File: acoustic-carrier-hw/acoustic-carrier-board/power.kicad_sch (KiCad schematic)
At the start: 88 parts, among them IC1 ECP5-BGA256, J3 Conn_02x08_Odd_Even, U10 TLV62569DBV, U11 TLV62569DBV, U14 TLV62569DBV, U5 OPA376xxDBV, U8 TLV62569DBV

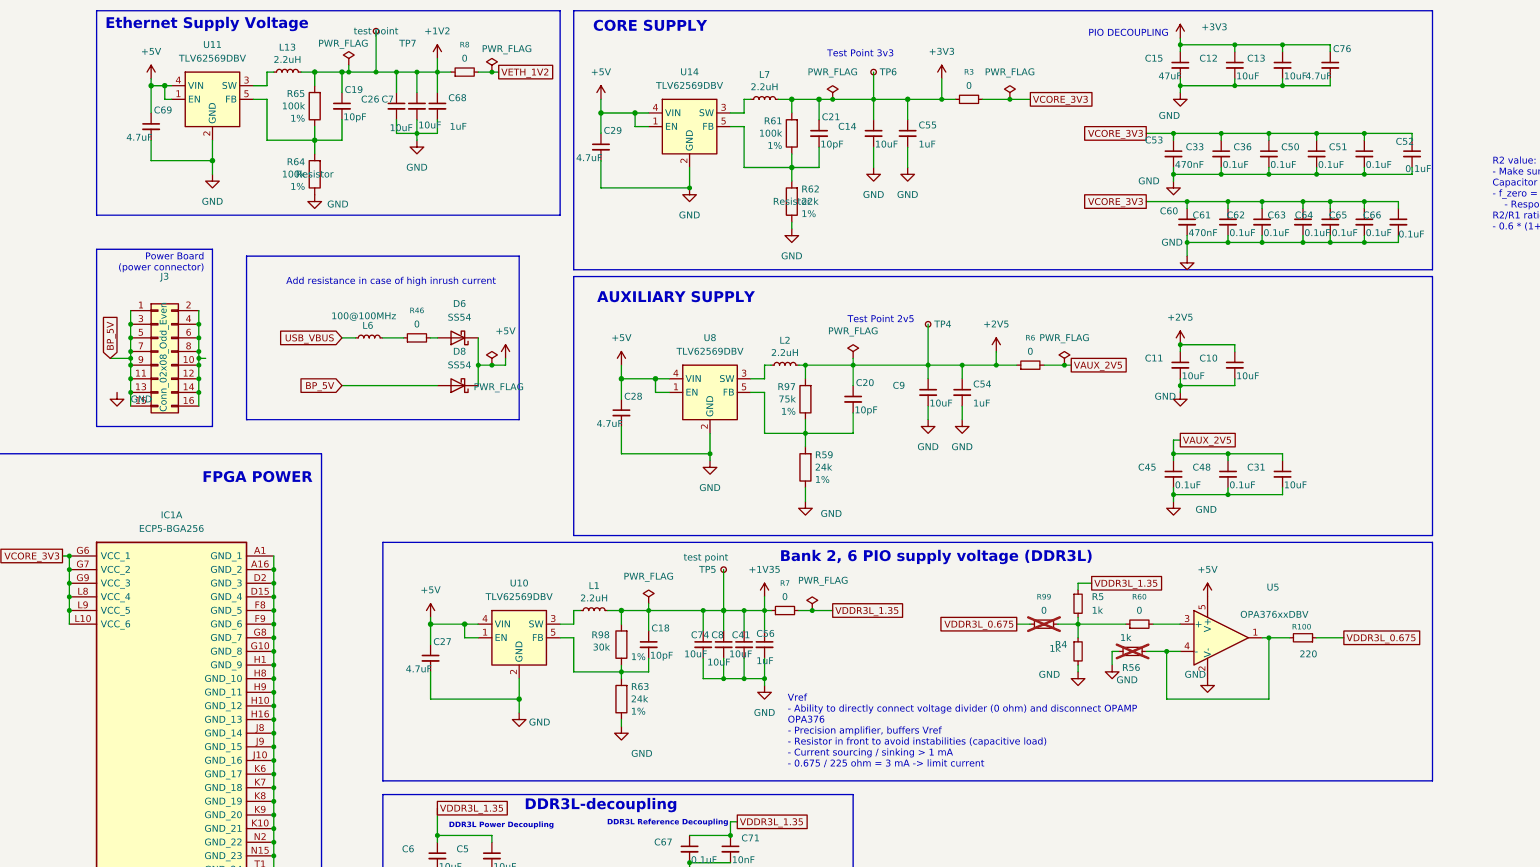
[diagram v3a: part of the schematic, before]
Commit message: [carrier] Checked power-supply part (next) check ethernet-board
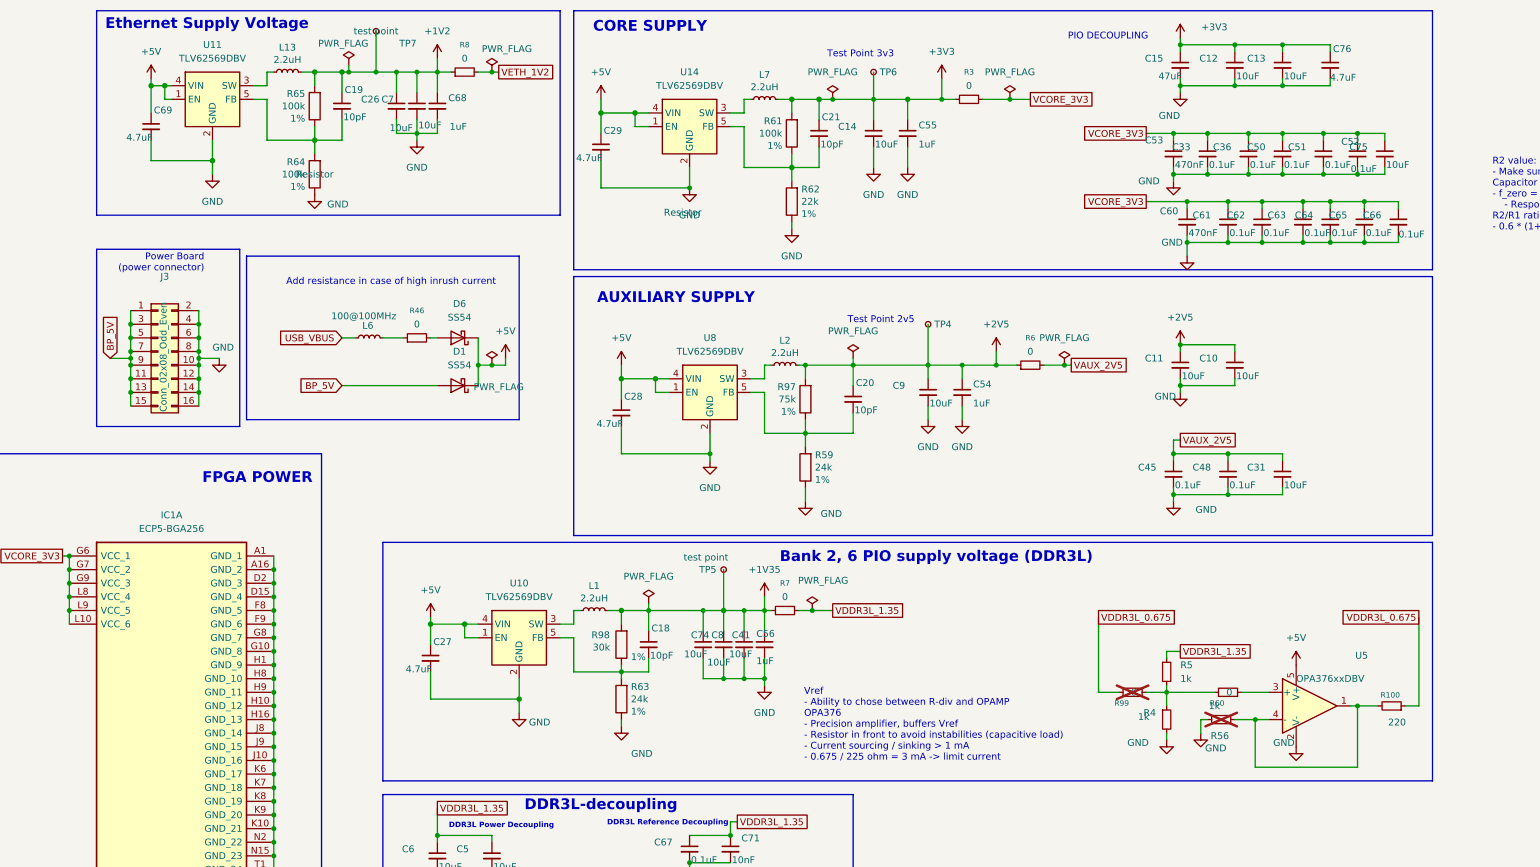
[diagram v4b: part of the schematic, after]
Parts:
- removed D8: SS54, Diode_SMD:D_SMA-SMB_Universal_Handsoldering, symbol Device:D_Schottky
- added C75: 10uF, Capacitor_SMD:C_0603_1608Metric, symbol Device:C_Small
- added D1: SS54, Diode_SMD:D_SMA, symbol Device:D_Schottky
- D6: footprint Diode_SMD:D_SMA-SMB_Universal_Handsoldering -> Diode_SMD:D_SMA
- R60, R99: footprint Resistor_SMD:R_0805_2012Metric_Pad1.20x1.40mm_HandSolder -> Resistor_SMD:R_0603_1608Metric; LPN C17477 -> C21189; MPN 0805W8F0000T5E -> 0603WAF0000T5E
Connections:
- net +5V: now also D1.1 (K)
- net BP_5V: now also D1.2 (A)
- net GND: now also J3.10 (Pin_10), J3.12 (Pin_12), J3.14 (Pin_14), J3.16 (Pin_16), J3.2 (Pin_2), J3.4 (Pin_4), J3.6 (Pin_6), J3.8 (Pin_8), C75.2
- net VCORE_3V3: now also C75.1
- net VDDR3L_0.675: now also R99.2; no longer R99.1
- net at R4.1, R5.2: now also R60.2, R99.1; no longer R60.1, R99.2
- net at U5.3 (+): now also R60.1; no longer R60.2
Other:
- note added: "Vref - Ability to chose between R-div and OPAMP OPA376 - Precision amplifier, buffers Vref - Resistor in front to avoid instabilities (capacitive load) - Current sourcing / sinking > 1 mA - 0.675 / 225 ohm = 3 mA -> limit current"
- note removed: "Vref - Ability to directly connect voltage divider (0 ohm) and disconnect OPAMP OPA376 - Precision amplifier, buffers Vref - Resistor in front to avoid instabilities (capacitive load) - Current sourcing / sinking > 1 mA - 0.675 / 225 ohm = 3 mA -> limit current"
- moved on the sheet: C33, C36, C50, C51, C52, R100, R4, R5, R56, U5

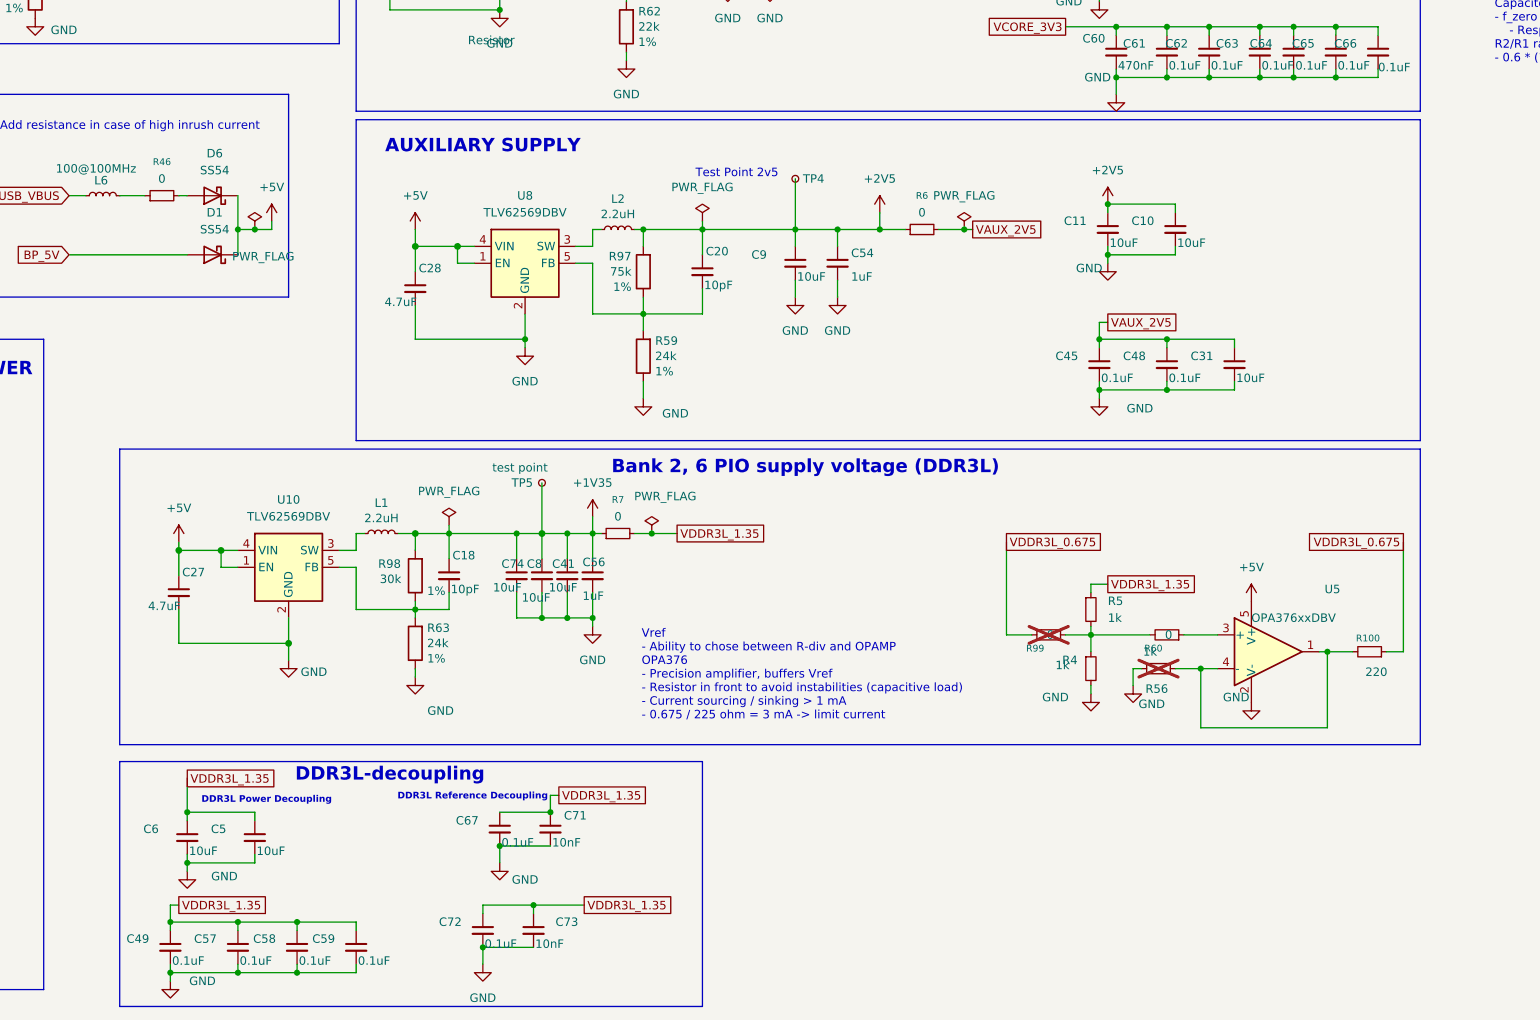
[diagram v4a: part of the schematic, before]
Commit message: [carrier] Added separate buses for ddr3 ctrl-cmd and dq-groups
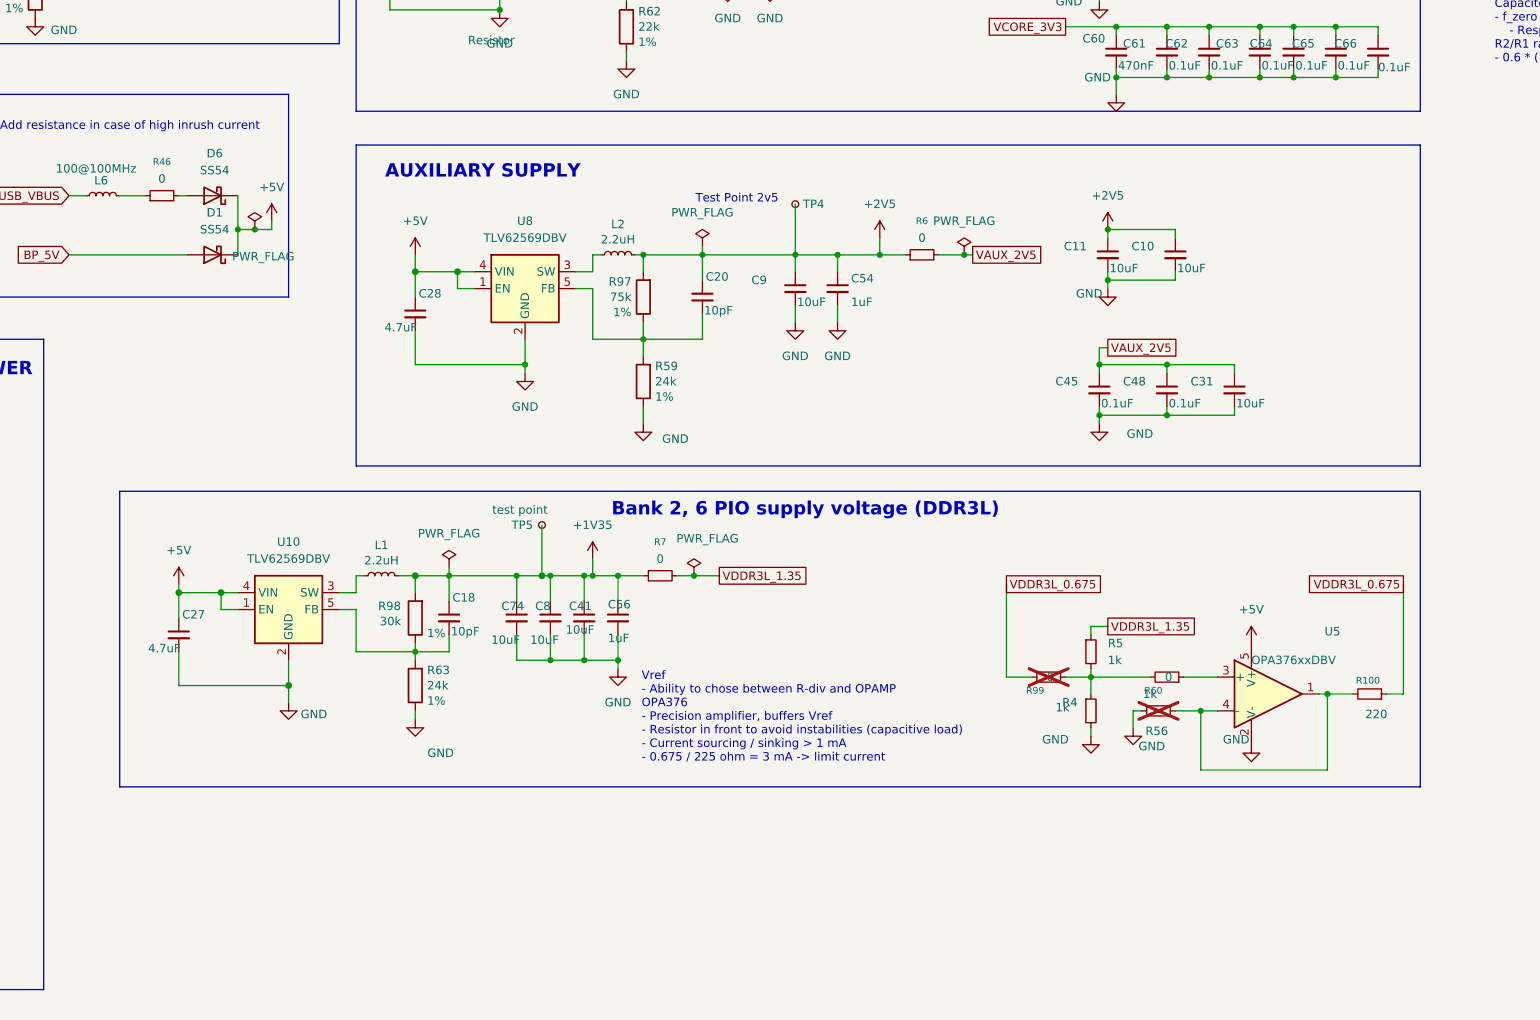
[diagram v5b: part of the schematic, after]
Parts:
- removed C49, C57, C58, C59, C67, C72: 0.1uF, Capacitor_SMD:C_0402_1005Metric, symbol Device:C_Small
- removed C5, C6: 10uF, Capacitor_SMD:C_0603_1608Metric, symbol Device:C_Small
- removed C71, C73: 10nF, Capacitor_SMD:C_0402_1005Metric, symbol Device:C_Small
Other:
- note removed: "DDR3L Power Decoupling"
- note removed: "DDR3L Reference Decoupling"
- note removed: "DDR3L-decoupling"
- moved on the sheet: C10, C11, C18, C20, C27, C28, C31, C41, C45, C48, C54, C56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

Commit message: [carrier] Reorganized schematic, moPut adc signals in bus, fixed DRC errors (next) recheck ethernet, check usb, add power switch
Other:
- moved on the sheet: C10, C11, C12, C13, C14, C15, C18, C19, C20, C21, C26, C27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

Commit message: [carrier] Fixed error in ethernet power supply, separated footprints + symbols into library (next) check whether supply should be DVDDH
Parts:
- removed IC1: ECP5-BGA256, fpga:BGA256C80P16X16_1400X1400X170, symbol ecp5bga256:ECP5-BGA256
- added IC1: ECP5-BGA256, iw-fpga_mcu:BGA256C80P16X16_1400X1400X170, symbol iw-fpga_mcu:ECP5-BGA256
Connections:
- net GND: now also IC1.A1 (GND_1), IC1.A16 (GND_2), IC1.D15 (GND_4), IC1.D2 (GND_3), IC1.F8 (GND_5), IC1.F9 (GND_6), IC1.G10 (GND_8), IC1.G8 (GND_7), IC1.H1 (GND_9), IC1.H10 (GND_12), IC1.H16 (GND_13), IC1.H8 (GND_10), IC1.H9 (GND_11), IC1.J10 (GND_16), IC1.J8 (GND_14), IC1.J9 (GND_15), IC1.K10 (GND_21), IC1.K6 (GND_17), IC1.K7 (GND_18), IC1.K8 (GND_19), IC1.K9 (GND_20), IC1.N15 (GND_23), IC1.N2 (GND_22), IC1.T1 (GND_24), IC1.T12 (GND_26), IC1.T16 (GND_27), IC1.T5 (GND_25)
- net VAUX_2V5: now also IC1.G11 (VCCAUX_1), IC1.L7 (VCCAUX_2)
- net VCORE_3V3: now also IC1.G6 (VCC_1), IC1.G7 (VCC_2), IC1.G9 (VCC_3), IC1.L10 (VCC_6), IC1.L8 (VCC_4), IC1.L9 (VCC_5)

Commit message: [¢arrier] Removed individual footprints and symbols
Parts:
- removed L13: 2.2uH, fpga:L_Changjiang_FNR4018S, symbol Device:L_Small
- added L3: 2.2uH, iw-inductor:L_Changjiang_FNR4018S, symbol Device:L_Small
- L1, L2, L7: footprint fpga:L_Changjiang_FNR4018S -> iw-inductor:L_Changjiang_FNR4018S
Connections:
- net +1V2: now also L3.2
- net at U11.3 (SW): now also L3.1
